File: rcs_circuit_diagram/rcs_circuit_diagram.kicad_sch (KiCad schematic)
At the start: 16 parts, among them J1 Conn_01x06_Pin, J2 Conn_01x02_Pin, J3 Conn_01x02_Pin, J4 Conn_01x02_Pin, J5 Conn_01x02_Pin, U1 LM2596S-5

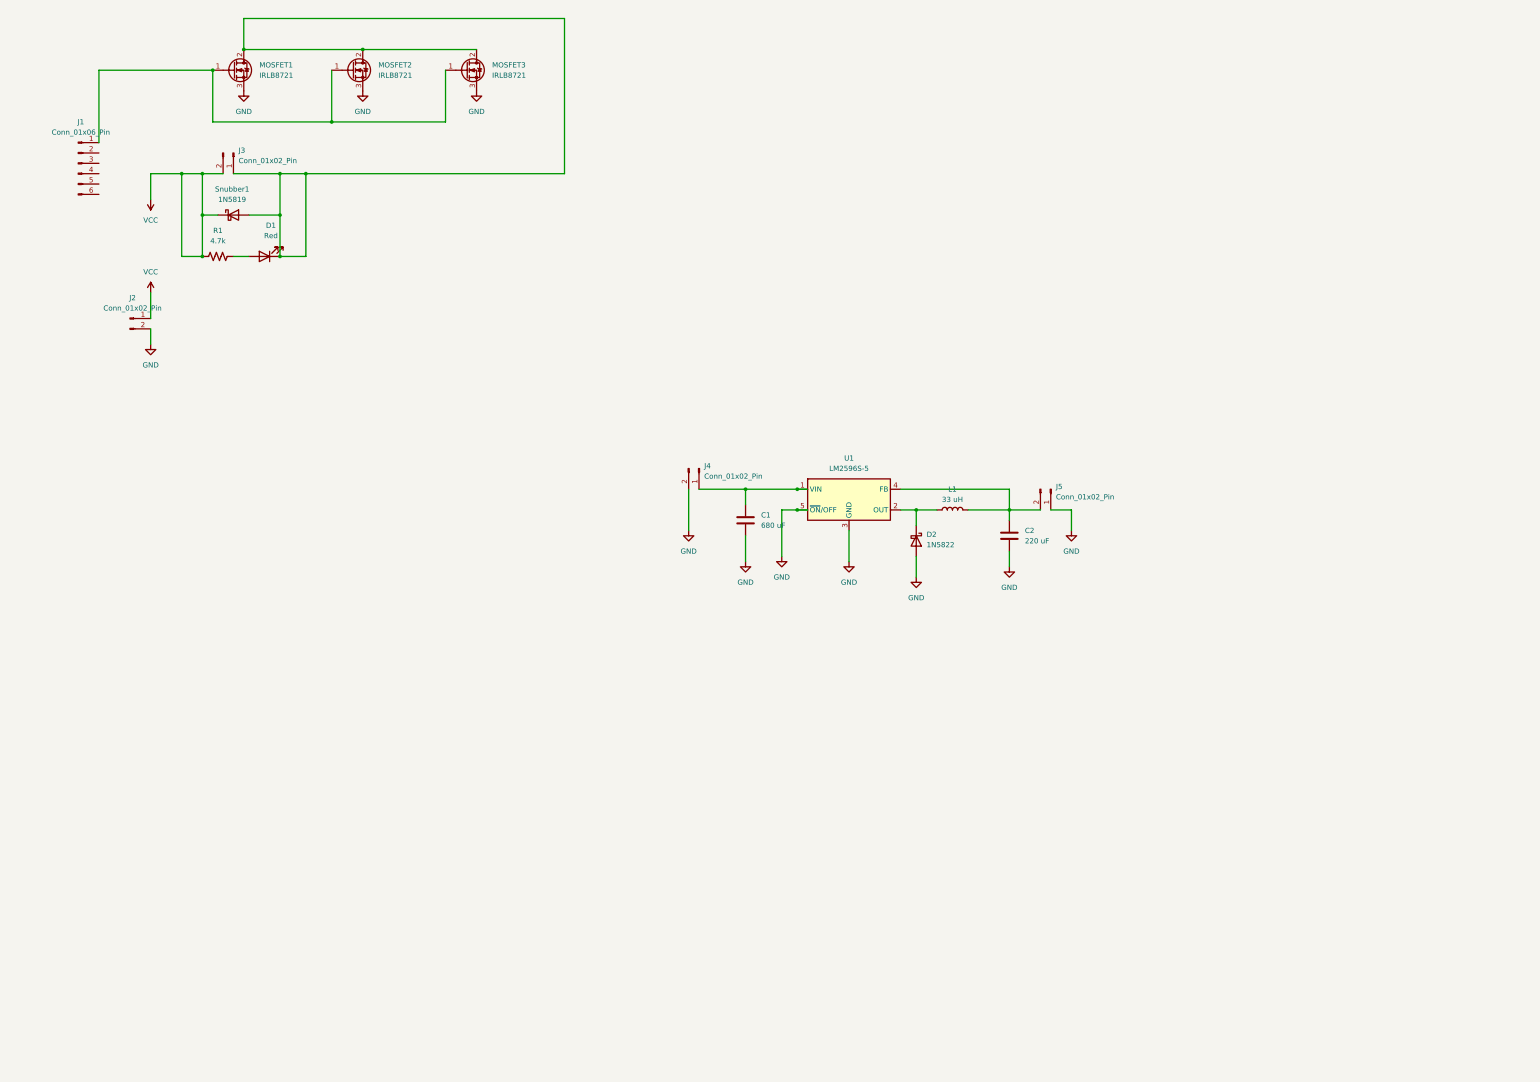
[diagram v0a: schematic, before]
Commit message: Duplicated the circuit for each solenoid
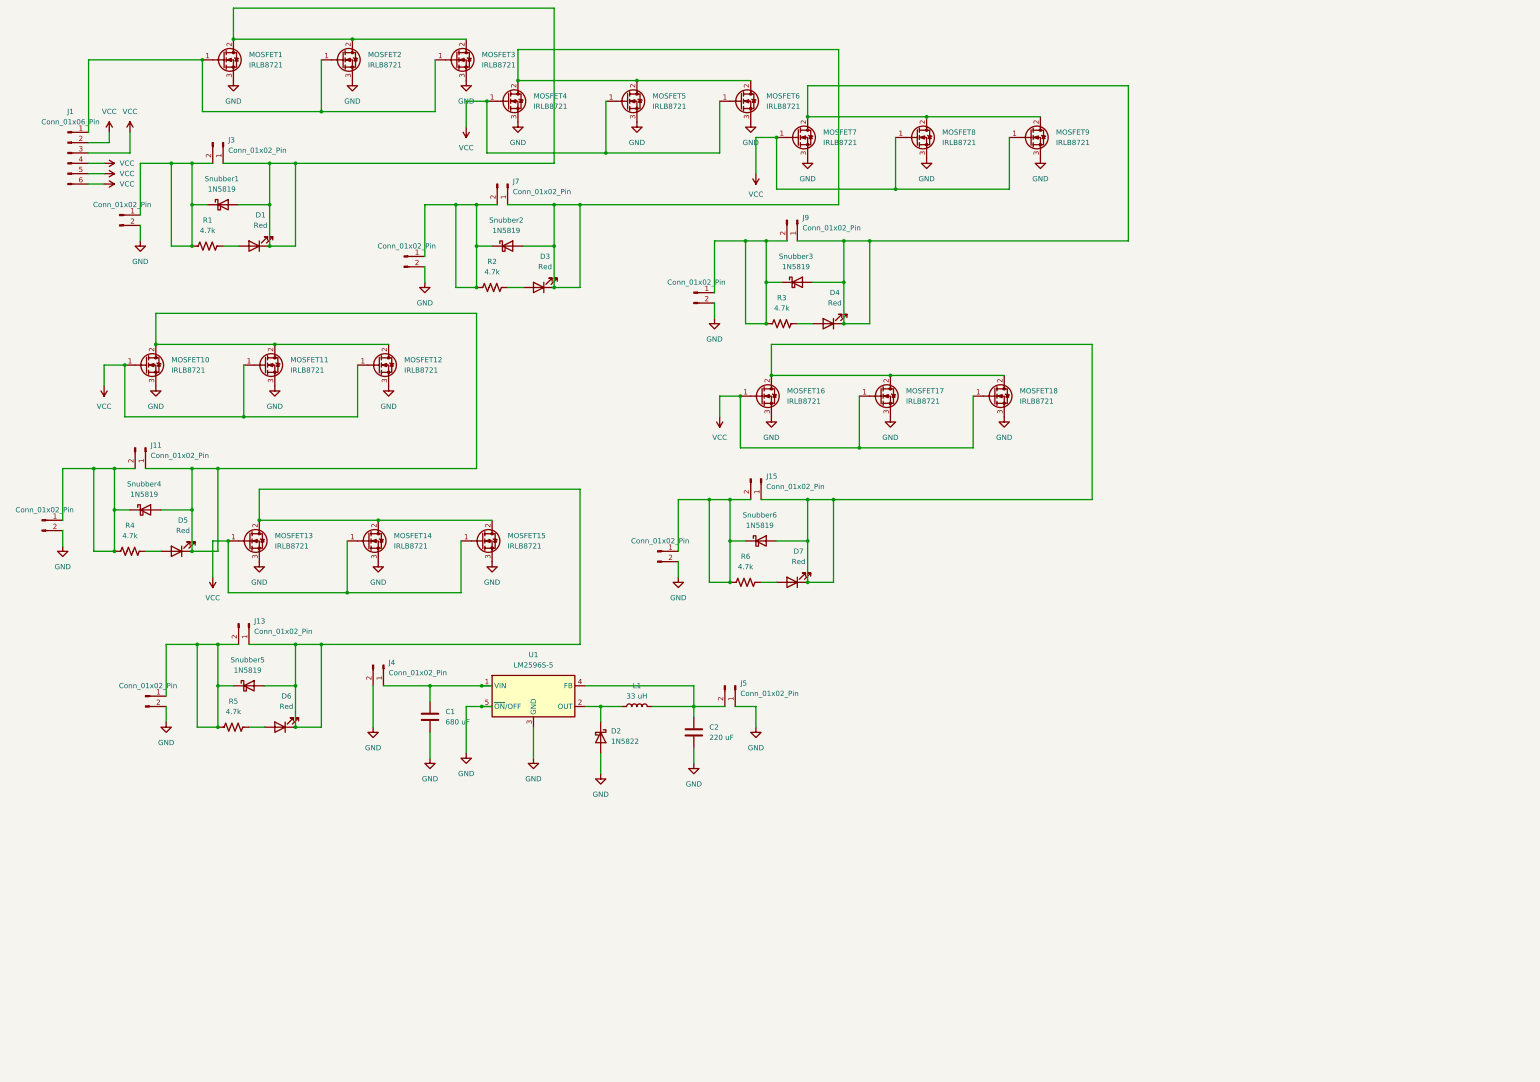
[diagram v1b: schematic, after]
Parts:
- added D3, D4, D5, D6, D7: Red, symbol Device:LED
- added J10, J11, J12, J13, J14, J15, J6, J7, J8, J9: Conn_01x02_Pin, symbol Connector:Conn_01x02_Pin
- added MOSFET10, MOSFET11, MOSFET12, MOSFET13, MOSFET14, MOSFET15, MOSFET16, MOSFET17, MOSFET18, MOSFET4, MOSFET5, MOSFET6, MOSFET7, MOSFET8, MOSFET9: IRLB8721, Package_TO_SOT_THT:TO-220-3_Vertical, symbol Transistor_FET:IRLB8721PBF
- added R2, R3, R4, R5, R6: 4.7k, symbol Device:R_US
- added Snubber2, Snubber3, Snubber4, Snubber5, Snubber6: 1N5819, Diode_THT:D_DO-41_SOD81_P10.16mm_Horizontal, symbol Diode:1N5819
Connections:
- net GND: now also J10.2 (Pin_2), J12.2 (Pin_2), J14.2 (Pin_2), J6.2 (Pin_2), J8.2 (Pin_2), MOSFET10.3 (S), MOSFET11.3 (S), MOSFET12.3 (S), MOSFET13.3 (S), MOSFET14.3 (S), MOSFET15.3 (S), MOSFET16.3 (S), MOSFET17.3 (S), MOSFET18.3 (S), MOSFET4.3 (S), MOSFET5.3 (S), MOSFET6.3 (S), MOSFET7.3 (S), MOSFET8.3 (S), MOSFET9.3 (S)
- net VCC: now also J1.2 (Pin_2), J1.3 (Pin_3), J1.4 (Pin_4), J1.5 (Pin_5), J1.6 (Pin_6), MOSFET10.1 (G), MOSFET11.1 (G), MOSFET12.1 (G), MOSFET13.1 (G), MOSFET14.1 (G), MOSFET15.1 (G), MOSFET16.1 (G), MOSFET17.1 (G), MOSFET18.1 (G), MOSFET4.1 (G), MOSFET5.1 (G), MOSFET6.1 (G), MOSFET7.1 (G), MOSFET8.1 (G), MOSFET9.1 (G); no longer J2.1 (Pin_1), J3.2 (Pin_2), R1.1, Snubber1.1 (K)
- new net: J14.1 (Pin_1), J15.2 (Pin_2), R6.1, Snubber6.1 (K)
- new net: D7.2 (A), R6.2
- new net: D3.1 (K), J7.1 (Pin_1), MOSFET4.2 (D), MOSFET5.2 (D), MOSFET6.2 (D), Snubber2.2 (A)
- new net: J12.1 (Pin_1), J13.2 (Pin_2), R5.1, Snubber5.1 (K)
- new net: D6.2 (A), R5.2
- new net: D6.1 (K), J13.1 (Pin_1), MOSFET13.2 (D), MOSFET14.2 (D), MOSFET15.2 (D), Snubber5.2 (A)
- new net: D4.1 (K), J9.1 (Pin_1), MOSFET7.2 (D), MOSFET8.2 (D), MOSFET9.2 (D), Snubber3.2 (A)
- new net: D5.1 (K), J11.1 (Pin_1), MOSFET10.2 (D), MOSFET11.2 (D), MOSFET12.2 (D), Snubber4.2 (A)
- new net: J10.1 (Pin_1), J11.2 (Pin_2), R4.1, Snubber4.1 (K)
- new net: J6.1 (Pin_1), J7.2 (Pin_2), R2.1, Snubber2.1 (K)
- new net: D4.2 (A), R3.2
- new net: D7.1 (K), J15.1 (Pin_1), MOSFET16.2 (D), MOSFET17.2 (D), MOSFET18.2 (D), Snubber6.2 (A)
- new net: D3.2 (A), R2.2
- new net: J2.1 (Pin_1), J3.2 (Pin_2), R1.1, Snubber1.1 (K)
- new net: D5.2 (A), R4.2
- new net: J8.1 (Pin_1), J9.2 (Pin_2), R3.1, Snubber3.1 (K)
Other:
- moved on the sheet: C1, C2, D1, D2, J1, J3, J4, J5, L1, MOSFET1, MOSFET2, MOSFET3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

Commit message: Cleaned up schematic
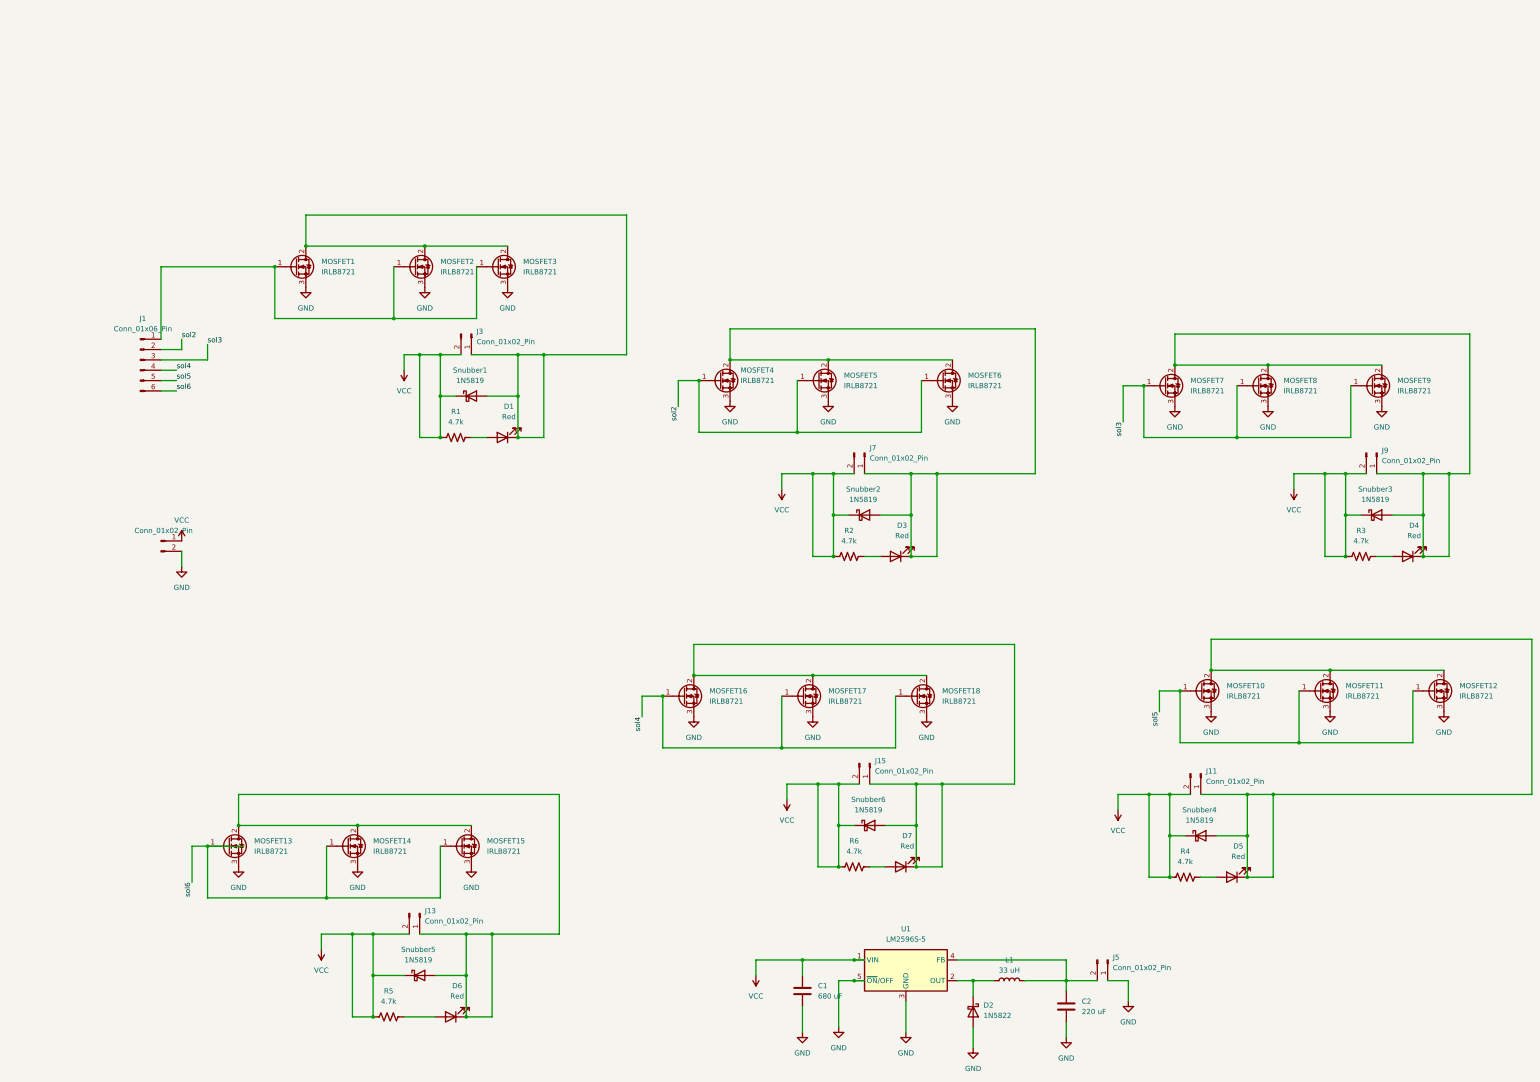
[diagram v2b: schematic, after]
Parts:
- removed J10, J12, J14, J2, J4, J8: Conn_01x02_Pin, symbol Connector:Conn_01x02_Pin
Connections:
- net VCC: now also C1.1, J11.2 (Pin_2), J13.2 (Pin_2), J15.2 (Pin_2), J3.2 (Pin_2), J6.1 (Pin_1), J7.2 (Pin_2), J9.2 (Pin_2), R1.1, R2.1, R3.1, R4.1, R5.1, R6.1, Snubber1.1 (K), Snubber2.1 (K), Snubber3.1 (K), Snubber4.1 (K), Snubber5.1 (K), Snubber6.1 (K), U1.1 (VIN); no longer J1.2 (Pin_2), J1.3 (Pin_3), J1.4 (Pin_4), J1.5 (Pin_5), J1.6 (Pin_6), MOSFET10.1 (G), MOSFET11.1 (G), MOSFET12.1 (G), MOSFET13.1 (G), MOSFET14.1 (G), MOSFET15.1 (G), MOSFET16.1 (G), MOSFET17.1 (G), MOSFET18.1 (G), MOSFET4.1 (G), MOSFET5.1 (G), MOSFET6.1 (G), MOSFET7.1 (G), MOSFET8.1 (G), MOSFET9.1 (G)
- new net sol2: J1.2 (Pin_2), MOSFET4.1 (G), MOSFET5.1 (G), MOSFET6.1 (G)
- new net sol3: J1.3 (Pin_3), MOSFET7.1 (G), MOSFET8.1 (G), MOSFET9.1 (G)
- new net sol4: J1.4 (Pin_4), MOSFET16.1 (G), MOSFET17.1 (G), MOSFET18.1 (G)
- new net sol5: J1.5 (Pin_5), MOSFET10.1 (G), MOSFET11.1 (G), MOSFET12.1 (G)
- new net sol6: J1.6 (Pin_6), MOSFET13.1 (G), MOSFET14.1 (G), MOSFET15.1 (G)
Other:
- moved on the sheet: C1, C2, D1, D2, D3, D4, D5, D6, D7, J1, J11, J13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
